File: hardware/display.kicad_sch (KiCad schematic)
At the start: 10 parts, among them J2 Conn_01x08_Pin, J3 Conn_01x08_Pin, J4 Conn_01x03_Pin, J5 Conn_01x02_Pin, U14 MM74HCT540MTCX, U4 MM74HCT541MTCX

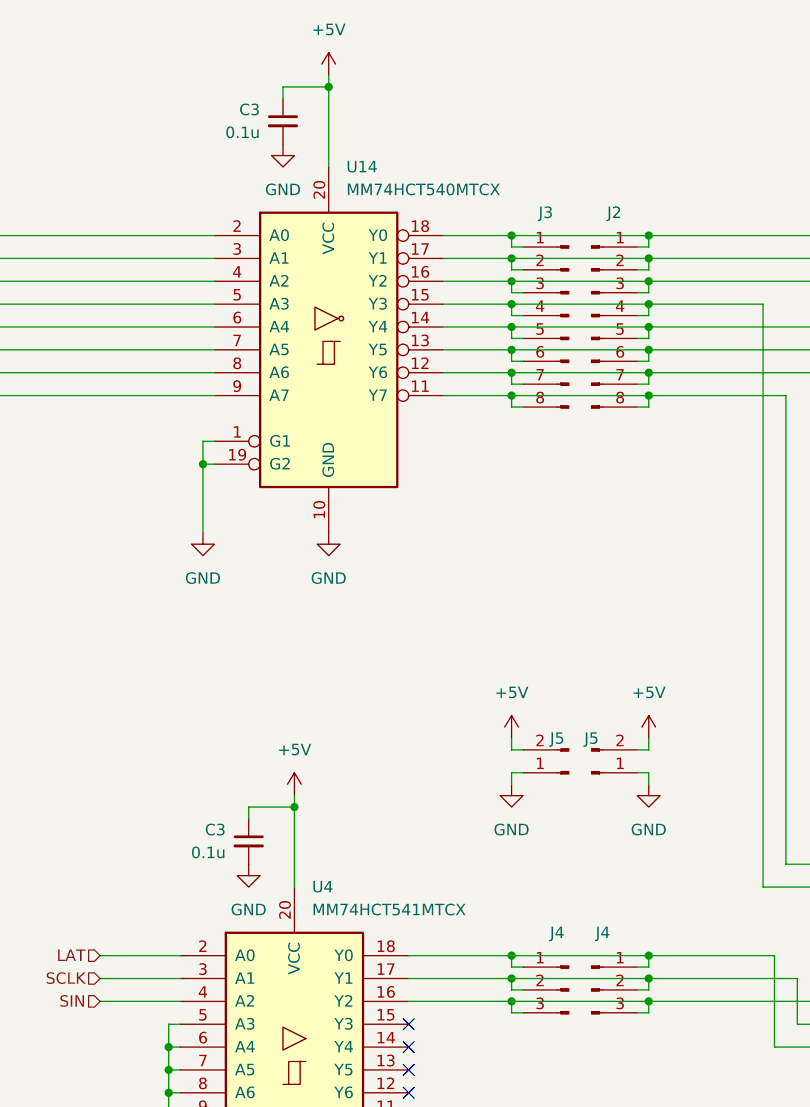
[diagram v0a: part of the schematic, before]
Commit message: Convert to PartDB
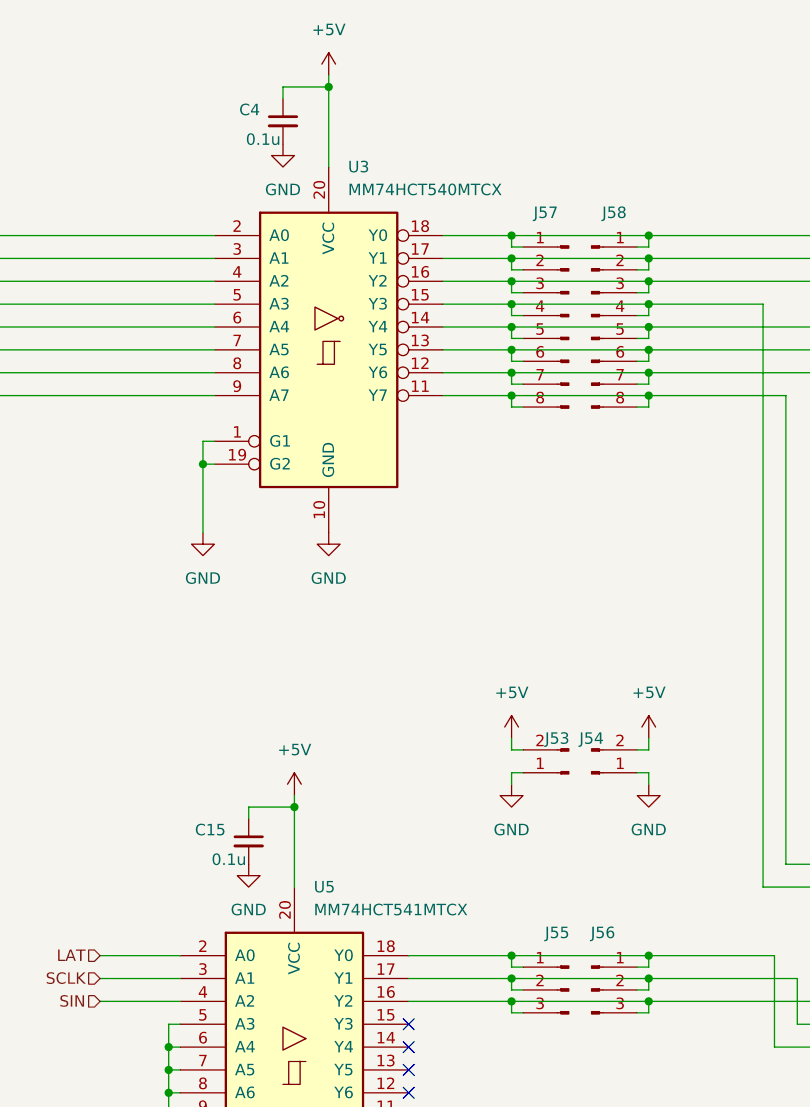
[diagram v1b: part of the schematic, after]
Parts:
- C15, C4: renamed from C3; symbol 0-passives:C-ceramic -> PartDB:C-Cer-0.1uF-25v-0603; Category (none) -> Capacitors/Ceramic; Manufacturer (none) -> Generic; Part-DB Footprint (none) -> 0603; Part-DB ID (none) -> 4; Part-DB URL (none) -> http://partdb.durbakyta.casa/en/part/4/info; Stock (none) -> 49; Storage Location (none) -> Main Parts Bin; manf (none) -> Generic
- U3: renamed from U14; symbol 0-74xx:74HCT540 -> PartDB:MM74HCT540MTCX; Category (none) -> IC/Logic; DigiKey SPN (none) -> MM74HCT540MTCXCT-ND; MPN (none) -> MM74HCT540MTCX; Manufacturer (none) -> onsemi; Manufacturing Status (none) -> Active; Part-DB ID (none) -> 86; Part-DB URL (none) -> http://partdb.durbakyta.casa/en/part/86/info; Stock (none) -> 1; Storage Location (none) -> Main Parts Bin; digikey# (none) -> MM74HCT540MTCXCT-ND; manf (none) -> onsemi; manf# (none) -> MM74HCT540MTCX
- U5: renamed from U4; symbol 74xx:74HCT541 -> PartDB:MM74HCT541MTCX; Category (none) -> IC/Logic; DigiKey SPN (none) -> MM74HCT541MTCXCT-ND; MPN (none) -> MM74HCT541MTCX; Manufacturer (none) -> onsemi; Manufacturing Status (none) -> Active; Part-DB ID (none) -> 85; Part-DB URL (none) -> http://partdb.durbakyta.casa/en/part/85/info; Stock (none) -> 1; Storage Location (none) -> Main Parts Bin; digikey# (none) -> MM74HCT541MTCXCT-ND; manf (none) -> onsemi; manf# (none) -> MM74HCT541MTCX
- renumbered J5 to J53, J5 to J54, J4 to J55, J4 to J56, J3 to J57, J2 to J58
